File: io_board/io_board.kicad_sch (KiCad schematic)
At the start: 54 parts, among them J1 RATE_CV1, J10 CLK_2, J11 SAW_2, J12 MIX, J13 IN2, J14 OUT2, J15 Conn_01x10_Male, J16 Conn_01x10_Male, J2 PWM_1, J3 CLK_1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

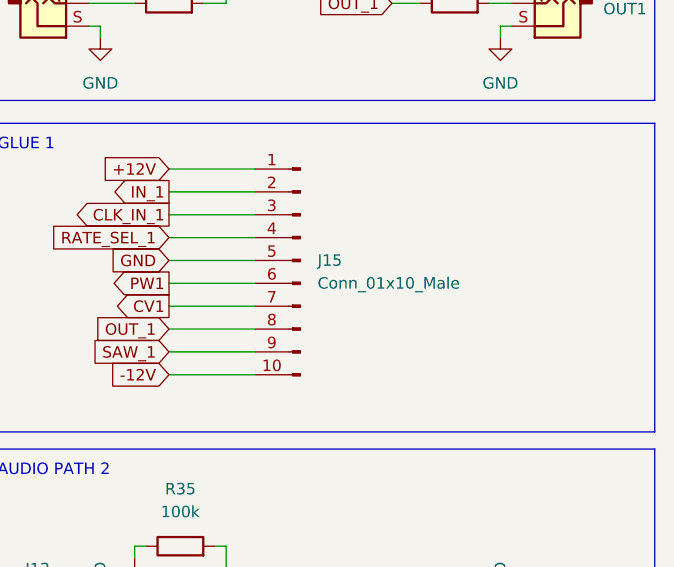
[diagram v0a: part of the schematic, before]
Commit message: Changed inputs to circles on panels
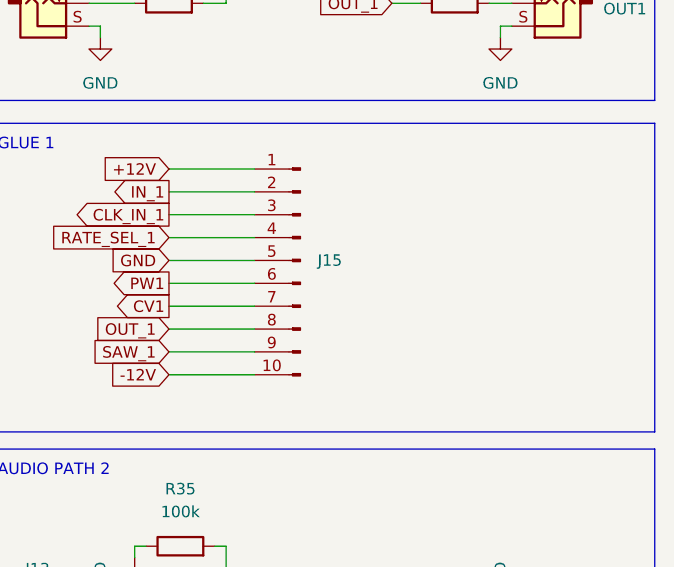
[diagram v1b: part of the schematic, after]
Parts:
- J15: value Conn_01x10_Male -> ~; footprint (none) -> Connector_PinHeader_2.54mm:PinHeader_1x10_P2.54mm_Vertical
- J16: footprint (none) -> Connector_PinHeader_2.54mm:PinHeader_1x10_P2.54mm_Vertical
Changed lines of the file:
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@@
       (effects (font (size 1.27 1.27)) (justify right))
     )
-    (property "Footprint" "" (id 2) (at 243.205 141.605 0)
+    (property "Footprint" "Connector_PinHeader_2.54mm:PinHeader_1x10_P2.54mm_Vertical" (id 2) (at 243.205 141.605 0)
       (effects (font (size 1.27 1.27)) hide)
     )
@@
       (effects (font (size 1.27 1.27)) (justify right))
     )
-    (property "Value" "Conn_01x10_Male" (id 1) (at 245.11 68.5799 0)
+    (property "Value" "~" (id 1) (at 245.11 68.5799 0)
       (effects (font (size 1.27 1.27)) (justify right))
     )
-    (property "Footprint" "" (id 2) (at 243.205 66.04 0)
+    (property "Footprint" "Connector_PinHeader_2.54mm:PinHeader_1x10_P2.54mm_Vertical" (id 2) (at 243.205 66.04 0)
       (effects (font (size 1.27 1.27)) hide)
     )
